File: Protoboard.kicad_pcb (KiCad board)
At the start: 2 copper layers, 100 x 138 mm, 76 parts, among them P1 CONN_01X08, P2 CONN_01X04, P3 CONN_01X05, P5 CONN_02X05, Q1 2N7000, U1 LoLin_V3

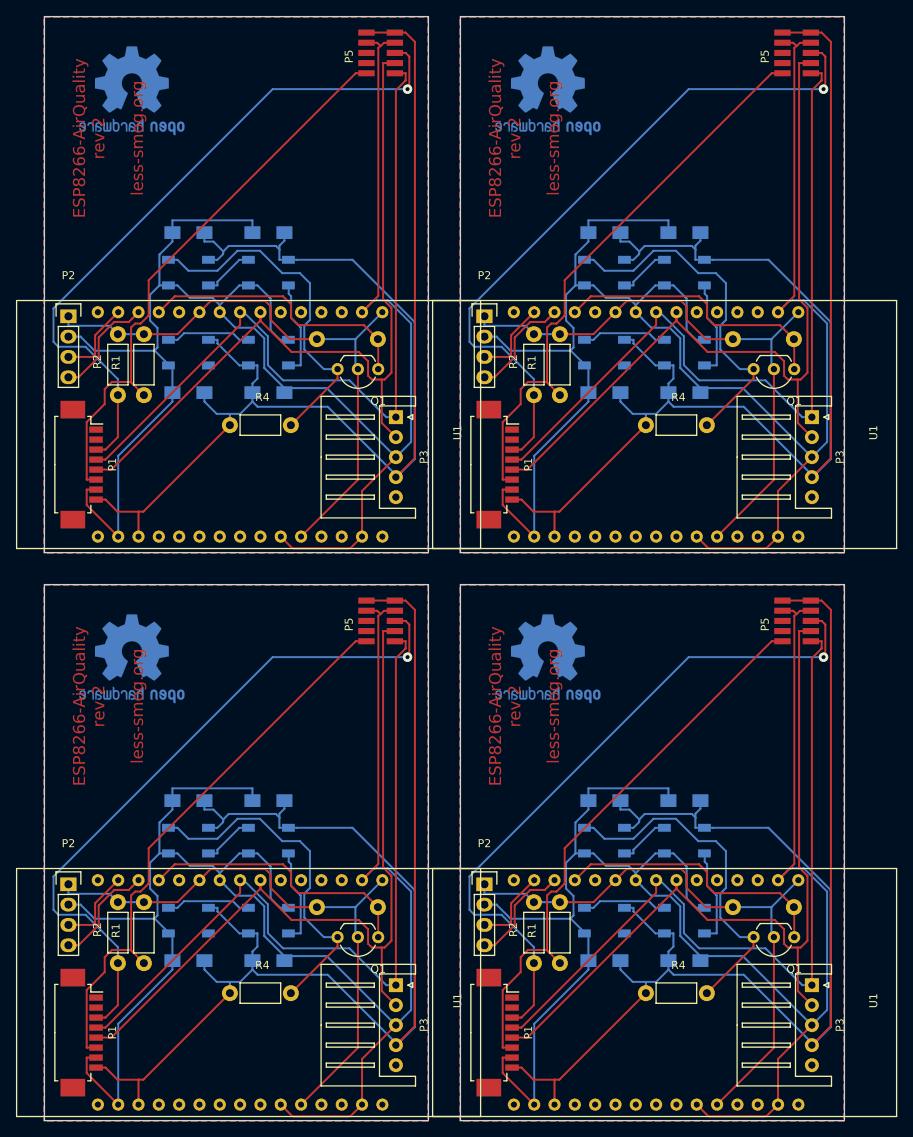
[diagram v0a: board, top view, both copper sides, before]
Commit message: Adjusted via sized for production.
Inner fi = 0.4mm min
Outer fi = 1.2mm min
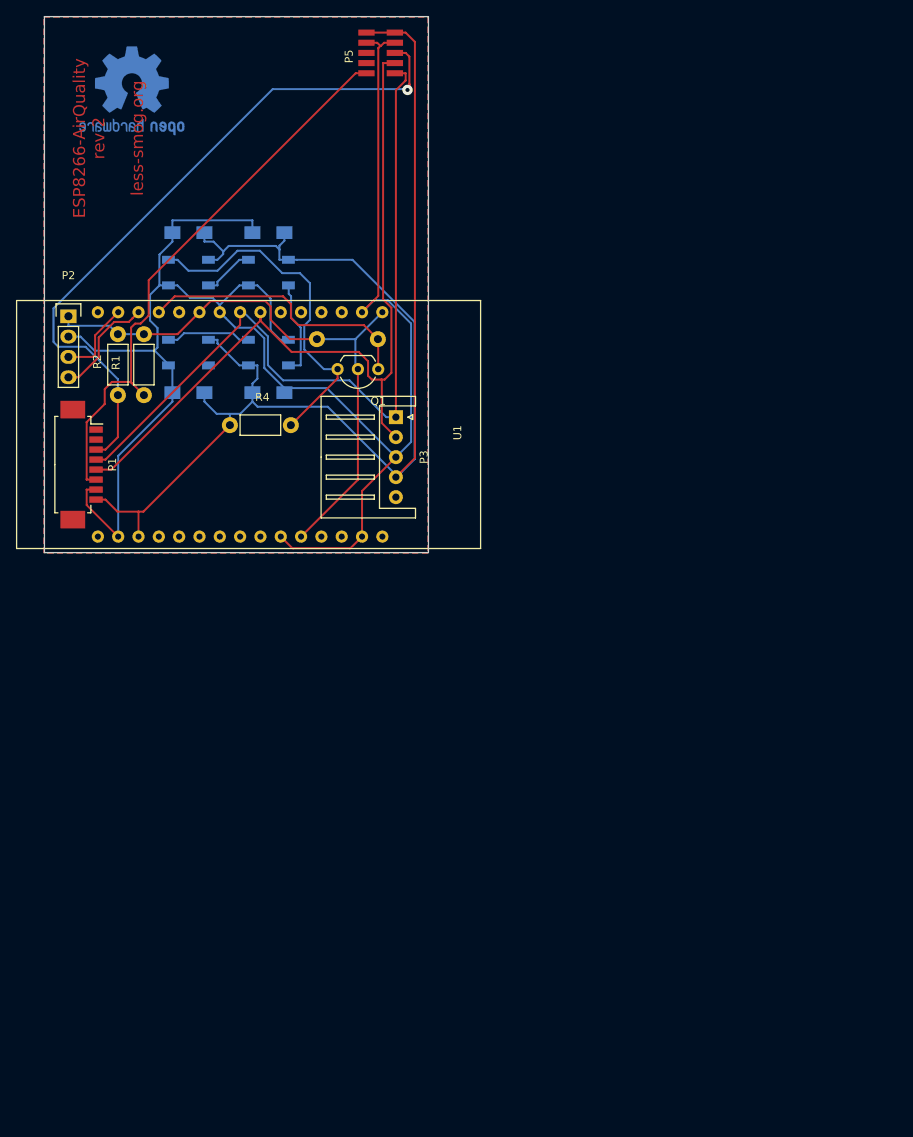
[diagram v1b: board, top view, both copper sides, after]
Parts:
- removed the C1 at (89.1, 117.9)
- removed the C1 at (37.1, 117.9)
- removed the C1 at (89.1, 46.9)
- removed the C2 at (99.1, 117.9)
- removed the C2 at (47.1, 117.9)
- removed the C2 at (99.1, 46.9)
- removed the C3 at (99.1, 137.9)
- removed the C3 at (47.1, 137.9)
- removed the C3 at (99.1, 66.9)
- removed the C4 at (89.1, 137.9)
- removed the C4 at (37.1, 137.9)
- removed the C4 at (89.1, 66.9)
- removed the LED1 at (89.1, 122.9)
- removed the LED1 at (37.1, 122.9)
- removed the LED1 at (89.1, 51.9)
- removed the LED2 at (99.1, 122.9)
- removed the LED2 at (47.1, 122.9)
- removed the LED2 at (99.1, 51.9)
- removed the LED3 at (99.1, 132.9)
- removed the LED3 at (47.1, 132.9)
- removed the LED3 at (99.1, 61.9)
- removed the LED4 at (89.1, 132.9)
- removed the LED4 at (37.1, 132.9)
- removed the LED4 at (89.1, 61.9)
- removed the P1 at (76.1, 146.9)
- removed the P1 at (24.1, 146.9)
- removed the P1 at (76.1, 75.9)
- removed the P2 at (74.1, 128.4)
- removed the P2 at (22.1, 128.4)
- removed the P2 at (74.1, 57.4)
- removed the P3 at (115.0, 141.0)
- removed the P3 at (63.0, 141.0)
- removed the P3 at (115.0, 70.0)
- removed the P5 at (111.3, 92.9)
- removed the P5 at (59.3, 92.9)
- removed the P5 at (111.3, 21.9)
- removed the Q1 at (112.8, 135.0)
- removed the Q1 at (60.8, 135.0)
- removed the Q1 at (112.8, 64.0)
- removed the R1 at (83.5, 138.2)
- removed the R1 at (31.5, 138.2)
- removed the R1 at (83.5, 67.2)
- removed the R2 at (80.2, 138.2)
- removed the R2 at (28.2, 138.2)
- removed the R2 at (80.2, 67.2)
- removed the R3 at (105.1, 131.2)
- removed the R3 at (53.1, 131.2)
- removed the R3 at (105.1, 60.2)
- removed the R4 at (94.2, 142.0)
- removed the R4 at (42.2, 142.0)
- removed the R4 at (94.2, 71.0)
- removed the REF*** at (82.0, 100.2)
- removed the REF*** at (30.0, 100.2)
- removed the REF*** at (82.0, 29.2)
- removed the U1 at (67.6, 157.7)
- removed the U1 at (15.6, 157.7)
- removed the U1 at (67.6, 86.7)
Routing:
- net GND: track 879.8 -> 220.0 mm
- net +5V: track 757.6 -> 189.4 mm
- net RXD: track 399.1 -> 99.8 mm
- net TXD: track 393.7 -> 98.4 mm
- net RESET: track 346.3 -> 86.7 mm, vias 4 -> 1
- net +3.3V: track 298.7 -> 74.7 mm
- net SET: track 287.0 -> 71.7 mm
- net LED: track 176.6 -> 44.2 mm
- net DIN: track 140.7 -> 35.2 mm
- net SCL: track 54.2 -> 13.6 mm
- net Net-(LED2-Pad2): track 48.7 -> 12.2 mm
- net Net-(LED3-Pad2): track 42.7 -> 10.7 mm
- net SDA: track 39.8 -> 9.96 mm
- net Net-(LED1-Pad2): track 26.4 -> 6.59 mm
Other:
- board size 100 x 138 mm -> 48 x 67 mm
